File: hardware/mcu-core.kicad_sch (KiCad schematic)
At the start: 22 parts, among them SW1 B3U-1000P, U1 STM32F103C8T6, Y1 12MHz

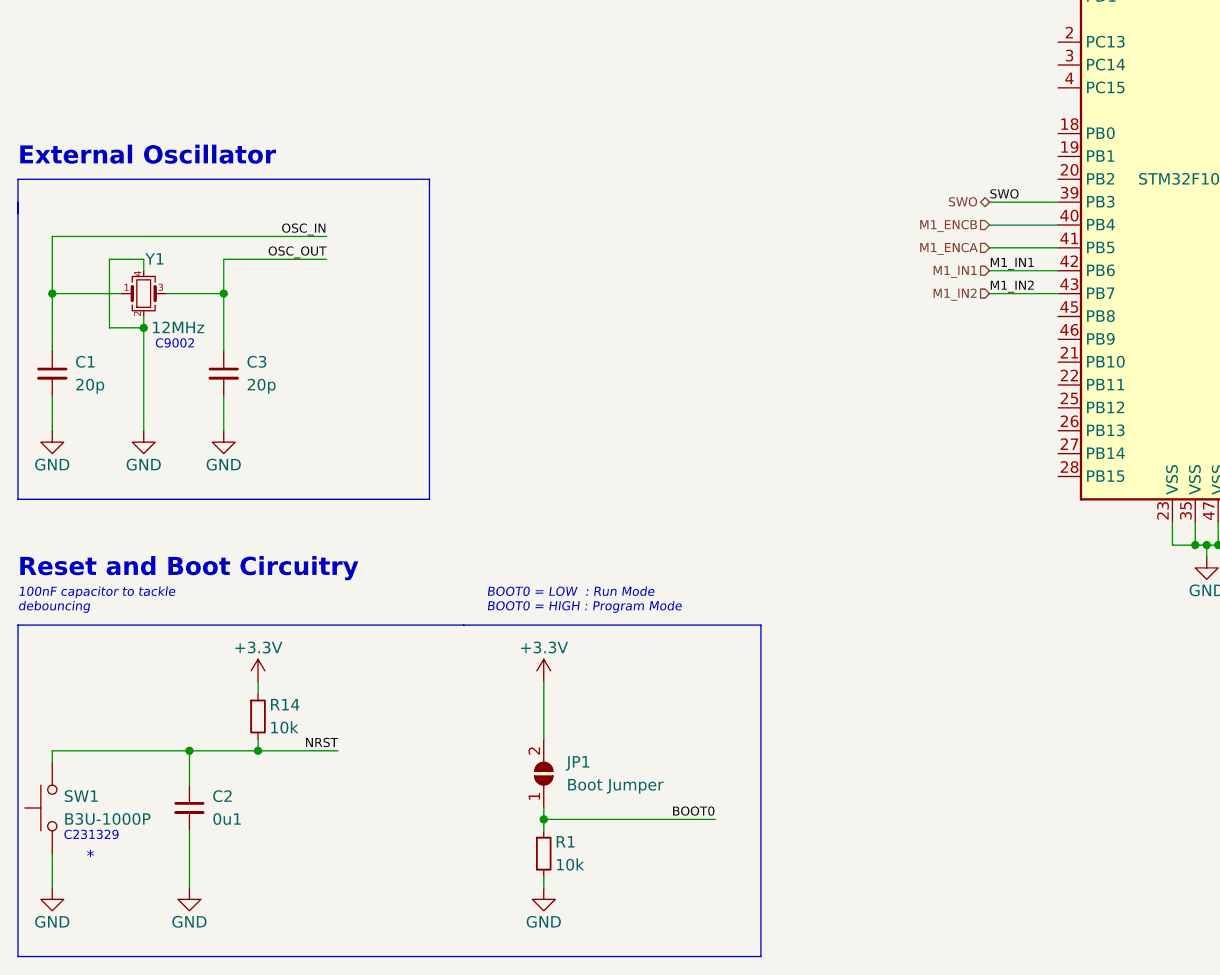
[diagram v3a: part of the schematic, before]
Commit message: Added BOOT1 jumper
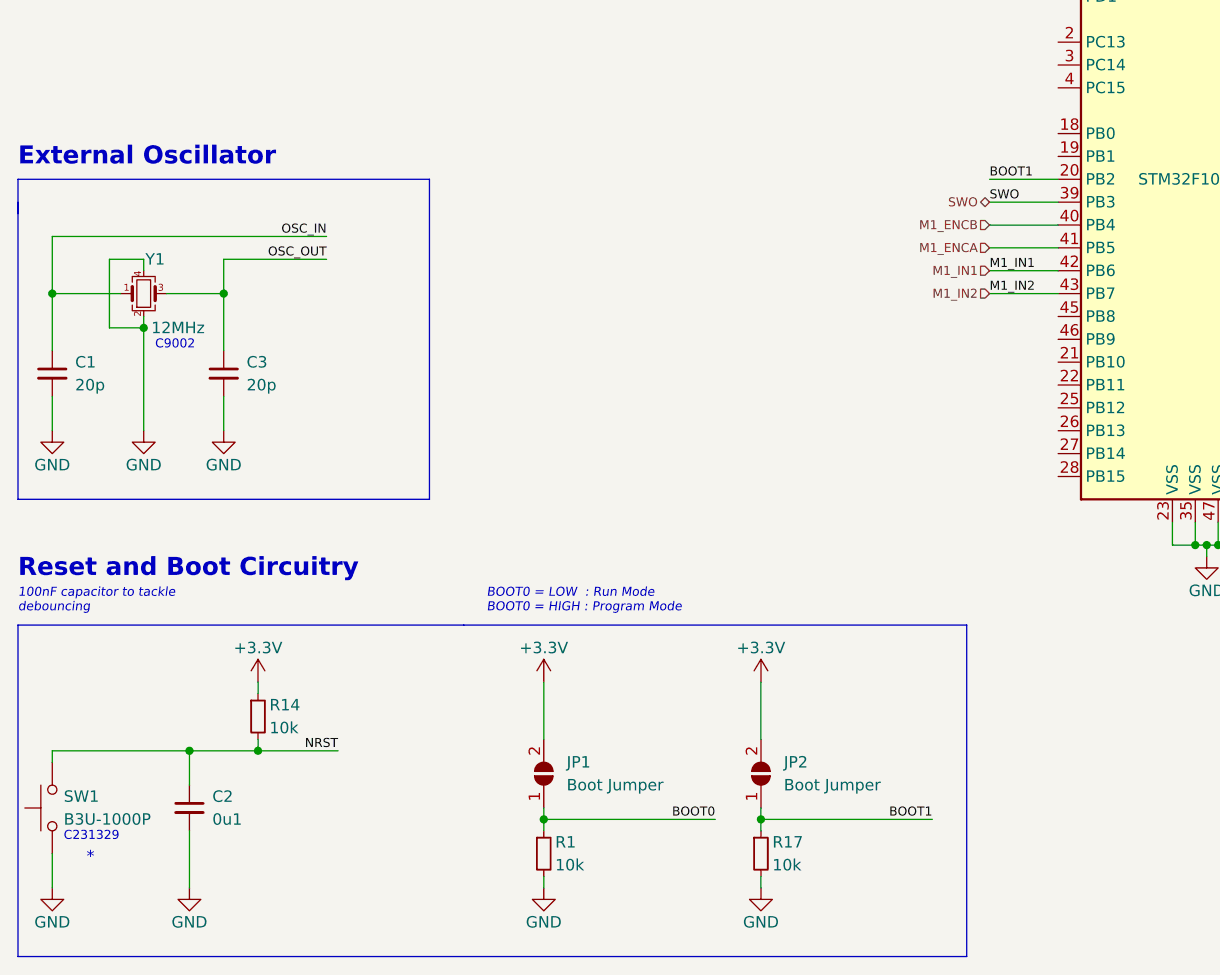
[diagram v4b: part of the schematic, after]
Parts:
- added JP2: Boot Jumper, Jumper:SolderJumper-2_P1.3mm_Open_Pad1.0x1.5mm, symbol Jumper:SolderJumper_2_Open
- added R17: 10k, Resistor_SMD:R_0402_1005Metric, symbol Device:R_Small
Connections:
- net +3.3V: now also JP2.2 (B)
- net GND: now also R17.2
- net BOOT1: now reaches U1.20 (PB2)
- net BOOT1: now also JP2.1 (A), R17.1
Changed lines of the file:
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@@
   (junction (at 125.73 66.04) (diameter 0) (color 0 0 0 0)
   )
+  (junction (at 96.52 181.61) (diameter 0) (color 0 0 0 0)
+  )
   (junction (at 40.64 173.99) (diameter 0) (color 0 0 0 0)
   )
@@
     (stroke (width 0) (type default) (color 0 0 0 0))
   )
+  (wire (pts (xy 96.52 181.61) (xy 96.52 182.88))
+    (stroke (width 0) (type default) (color 0 0 0 0))
+  )
   (wire (pts (xy 36.83 119.38) (xy 48.26 119.38))
     (stroke (width 0) (type default) (color 0 0 0 0))
@@
     (stroke (width 0) (type default) (color 0 0 0 0))
   )
+  (wire (pts (xy 96.52 181.61) (xy 115.57 181.61))
+    (stroke (width 0) (type default) (color 0 0 0 0))
+  )
   (wire (pts (xy 121.92 120.65) (xy 129.54 120.65))
     (stroke (width 0) (type default) (color 0 0 0 0))
@@
     (stroke (width 0) (type default) (color 0 0 0 0))
   )
+  (wire (pts (xy 96.52 180.34) (xy 96.52 181.61))
+    (stroke (width 0) (type default) (color 0 0 0 0))
+  )
   (wire (pts (xy 121.92 115.57) (xy 129.54 115.57))
     (stroke (width 0) (type default) (color 0 0 0 0))
@@
     (stroke (width 0) (type default) (color 0 0 0 0))
   )
-  (polyline (pts (xy 96.52 160.02) (xy 96.52 196.85))
+  (polyline (pts (xy 119.38 160.02) (xy 119.38 196.85))
     (stroke (width 0) (type default) (color 0 0 0 0))
   )
@@
     (stroke (width 0) (type default) (color 0 0 0 0))
   )
+  (wire (pts (xy 96.52 187.96) (xy 96.52 189.23))
+    (stroke (width 0) (type default) (color 0 0 0 0))
+  )
   (polyline (pts (xy 59.69 146.05) (xy 59.69 110.49))
     (stroke (width 0) (type default) (color 0 0 0 0))
   )
-  (polyline (pts (xy 63.5 160.02) (xy 96.52 160.02))
+  (polyline (pts (xy 63.5 160.02) (xy 119.38 160.02))
     (stroke (width 0) (type default) (color 0 0 0 0))
   )
@@
     (stroke (width 0) (type default) (color 0 0 0 0))
   )
+  (wire (pts (xy 96.52 166.37) (xy 96.52 172.72))
+    (stroke (width 0) (type default) (color 0 0 0 0))
+  )
   (wire (pts (xy 162.56 133.35) (xy 177.8 133.35))
     (stroke (width 0) (type default) (color 0 0 0 0))
@@
     (stroke (width 0) (type default) (color 0 0 0 0))
   )
+  (wire (pts (xy 121.92 110.49) (xy 129.54 110.49))
+    (stroke (width 0) (type default) (color 0 0 0 0))
+  )
   (wire (pts (xy 146.05 152.4) (xy 146.05 151.13))
     (stroke (width 0) (type default) (color 0 0 0 0))
@@
     (stroke (width 0) (type default) (color 0 0 0 0))
   )
-  (polyline (pts (xy 96.52 196.85) (xy 13.97 196.85))
+  (polyline (pts (xy 119.38 196.85) (xy 13.97 196.85))
     (stroke (width 0) (type default) (color 0 0 0 0))
   )
@@
     (effects (font (size 1 1)) (justify right bottom))
   )
+  (label "BOOT1" (at 121.92 110.49 0)
+    (effects (font (size 1 1)) (justify left bottom))
+  )
   (label "OSC_IN" (at 48.26 116.84 180)
     (effects (font (size 1 1)) (justify right bottom))
@@
   (label "NRST" (at 119.38 77.47 0)
     (effects (font (size 1 1)) (justify left bottom))
+  )
+  (label "BOOT1" (at 115.57 181.61 180)
+    (effects (font (size 1 1)) (justify right bottom))
   )
   (label "BOOT0" (at 91.44 181.61 180)
@@
     )
     (pin "1")
+  )
+  (symbol (lib_id "Device:R_Small") (at 96.52 185.42 0) (unit 1)
+    (in_bom yes) (on_board yes)
+    (property "Reference" "R17" (id 0) (at 97.79 184.15 0)
+      (effects (font (size 1.27 1.27)) (justify left))
+    )
+    (property "Value" "10k" (id 1) (at 97.79 186.69 0)
+      (effects (font (size 1.27 1.27)) (justify left))
+    )
+    (property "Footprint" "Resistor_SMD:R_0402_1005Metric" (id 2) (at 96.52 185.42 0)
+      (effects (font (size 1.27 1.27)) hide)
+    )
+    (property "Datasheet" "~" (id 3) (at 96.52 185.42 0)
+      (effects (font (size 1.27 1.27)) hide)
+    )
+    (pin "1")
+    (pin "2")
   )
   (symbol (lib_id "Switch:SW_Push") (at 17.78 180.34 90) (unit 1)
@@
     (pin "4")
   )
+  (symbol (lib_id "power:GND") (at 96.52 189.23 0) (unit 1)
+    (in_bom yes) (on_board yes)
+    (property "Reference" "#PWR056" (id 0) (at 96.52 195.58 0)
+      (effects (font (size 1.27 1.27)) hide)
+    )
+    (property "Value" "GND" (id 1) (at 96.52 193.04 0))
+    (property "Footprint" "" (id 2) (at 96.52 189.23 0)
+      (effects (font (size 1.27 1.27)) hide)
+    )
+    (property "Datasheet" "" (id 3) (at 96.52 189.23 0)
+      (effects (font (size 1.27 1.27)) hide)
+    )
+    (pin "1")
+  )
   (symbol (lib_id "power:+3.3V") (at 190.5 125.73 0) (unit 1)
     (in_bom yes) (on_board yes)
@@
     )
     (property "Datasheet" "~" (id 3) (at 256.54 100.33 0)
+      (effects (font (size 1.27 1.27)) hide)
+    )
+    (pin "1")
+    (pin "2")
+  )
+  (symbol (lib_id "Jumper:SolderJumper_2_Open") (at 96.52 176.53 90) (unit 1)
+    (in_bom yes) (on_board yes) (fields_autoplaced)
+    (property "Reference" "JP2" (id 0) (at 99.06 175.2599 90)
+      (effects (font (size 1.27 1.27)) (justify right))
+    )
+    (property "Value" "Boot Jumper" (id 1) (at 99.06 177.7999 90)
+      (effects (font (size 1.27 1.27)) (justify right))
+    )
+    (property "Footprint" "Jumper:SolderJumper-2_P1.3mm_Open_Pad1.0x1.5mm" (id 2) (at 96.52 176.53 0)
+      (effects (font (size 1.27 1.27)) hide)
+    )
+    (property "Datasheet" "~" (id 3) (at 96.52 176.53 0)
       (effects (font (size 1.27 1.27)) hide)
     )
@@
       (effects (font (size 1.27 1.27)) hide)
     )
+    (pin "1")
+  )
+  (symbol (lib_id "power:+3.3V") (at 96.52 166.37 0) (unit 1)
+    (in_bom yes) (on_board yes)
+    (property "Reference" "#PWR055" (id 0) (at 96.52 170.18 0)
+      (effects (font (size 1.27 1.27)) hide)
+    )
+    (property "Value" "+3.3V" (id 1) (at 96.52 162.56 0))
+    (property "Footprint" "" (id 2) (at 96.52 166.37 0)
+      (effects (font (size 1.27 1.27)) hide)
+    )
+    (property "Datasheet" "" (id 3) (at 96.52 166.37 0)
+      (effects (font (size 1.27 1.27)) hide)
+    )

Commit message: Added status LED and silkscreen
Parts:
- added D15: orange, LED_SMD:LED_0603_1608Metric, symbol Device:LED_Small_Filled
- added R18: 1k5, Resistor_SMD:R_0402_1005Metric, symbol Device:R_Small
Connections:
- net GND: now also R18.2
- net at U1.27 (PB14): now also D15.2 (A)
- new net: D15.1 (K), R18.1
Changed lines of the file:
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@@
+    (stroke (width 0) (type default) (color 0 0 0 0))
+  )
+  (wire (pts (xy 118.11 140.97) (xy 118.11 142.24))
     (stroke (width 0) (type default) (color 0 0 0 0))
   )
@@
     (stroke (width 0) (type default) (color 0 0 0 0))
   )
+  (wire (pts (xy 118.11 140.97) (xy 129.54 140.97))
+    (stroke (width 0) (type default) (color 0 0 0 0))
+  )
   (wire (pts (xy 96.52 181.61) (xy 115.57 181.61))
     (stroke (width 0) (type default) (color 0 0 0 0))
@@
     (stroke (width 0) (type default) (color 0 0 0 0))
   )
+  (wire (pts (xy 118.11 147.32) (xy 118.11 148.59))
+    (stroke (width 0) (type default) (color 0 0 0 0))
+  )
   (wire (pts (xy 144.78 151.13) (xy 142.24 151.13))
     (stroke (width 0) (type default) (color 0 0 0 0))
@@
   )
   (wire (pts (xy 101.6 66.04) (xy 101.6 67.31))
+    (stroke (width 0) (type default) (color 0 0 0 0))
+  )
+  (wire (pts (xy 118.11 153.67) (xy 118.11 154.94))
     (stroke (width 0) (type default) (color 0 0 0 0))
   )
@@
     (pin "2")
   )
+  (symbol (lib_id "Device:LED_Small_Filled") (at 118.11 144.78 90) (unit 1)
+    (in_bom yes) (on_board yes)
+    (property "Reference" "D15" (id 0) (at 113.03 143.51 90)
+      (effects (font (size 1.27 1.27)) (justify right))
+    )
+    (property "Value" "orange" (id 1) (at 110.49 147.32 90)
+      (effects (font (size 1.27 1.27)) (justify right))
+    )
+    (property "Footprint" "LED_SMD:LED_0603_1608Metric" (id 2) (at 118.11 144.78 90)
+      (effects (font (size 1.27 1.27)) hide)
+    )
+    (property "Datasheet" "~" (id 3) (at 118.11 144.78 90)
+      (effects (font (size 1.27 1.27)) hide)
+    )
+    (pin "1")
+    (pin "2")
+  )
   (symbol (lib_id "Device:R_Small") (at 72.39 185.42 0) (unit 1)
     (in_bom yes) (on_board yes)
@@
     (pin "2")
   )
+  (symbol (lib_id "power:GND") (at 118.11 154.94 0) (unit 1)
+    (in_bom yes) (on_board yes)
+    (property "Reference" "#PWR057" (id 0) (at 118.11 161.29 0)
+      (effects (font (size 1.27 1.27)) hide)
+    )
+    (property "Value" "GND" (id 1) (at 118.11 158.75 0))
+    (property "Footprint" "" (id 2) (at 118.11 154.94 0)
+      (effects (font (size 1.27 1.27)) hide)
+    )
+    (property "Datasheet" "" (id 3) (at 118.11 154.94 0)
+      (effects (font (size 1.27 1.27)) hide)
+    )
+    (pin "1")
+  )
   (symbol (lib_id "power:GND") (at 72.39 189.23 0) (unit 1)
     (in_bom yes) (on_board yes)
@@
     (pin "1")
   )
+  (symbol (lib_id "Device:R_Small") (at 118.11 151.13 0) (mirror y) (unit 1)
+    (in_bom yes) (on_board yes)
+    (property "Reference" "R18" (id 0) (at 116.84 149.86 0)
+      (effects (font (size 1.27 1.27)) (justify left))
+    )
+    (property "Value" "1k5" (id 1) (at 116.84 152.4 0)
+      (effects (font (size 1.27 1.27)) (justify left))
+    )
+    (property "Footprint" "Resistor_SMD:R_0402_1005Metric" (id 2) (at 118.11 151.13 0)
+      (effects (font (size 1.27 1.27)) hide)
+    )
+    (property "Datasheet" "~" (id 3) (at 118.11 151.13 0)
+      (effects (font (size 1.27 1.27)) hide)
+    )
+    (pin "1")
+    (pin "2")
+  )
   (symbol (lib_id "power:GND") (at 17.78 189.23 0) (unit 1)

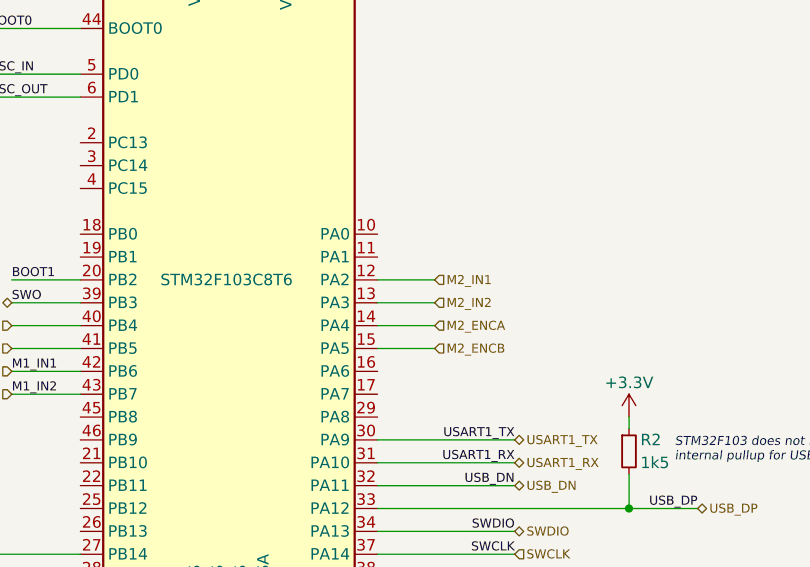
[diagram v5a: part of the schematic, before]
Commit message: Minor changes, added 100n cap
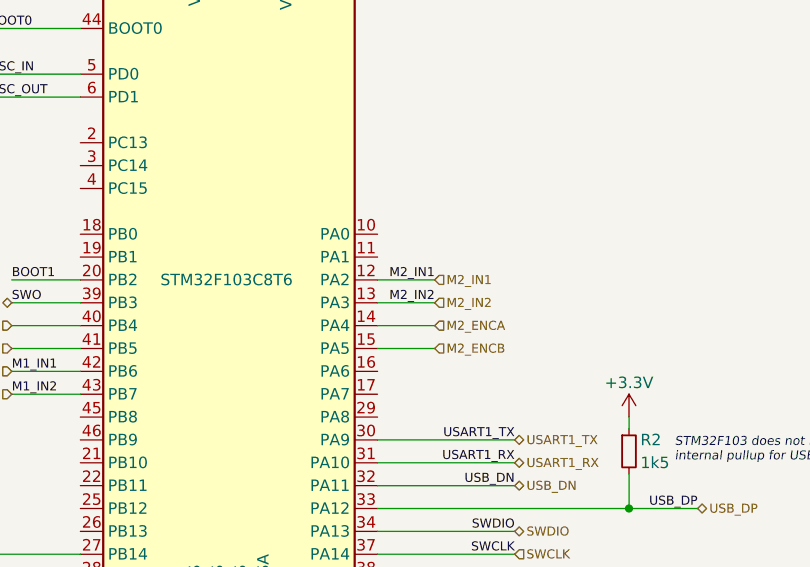
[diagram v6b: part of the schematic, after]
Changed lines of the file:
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@@
+    (effects (font (size 1 1)) (justify right bottom))
+  )
+  (label "M2_IN2" (at 168.91 113.03 180)
     (effects (font (size 1 1)) (justify right bottom))
   )
@@
     (effects (font (size 1 1)) (justify right bottom))
   )
+  (label "M2_IN1" (at 168.91 110.49 180)
+    (effects (font (size 1 1)) (justify right bottom))
+  )

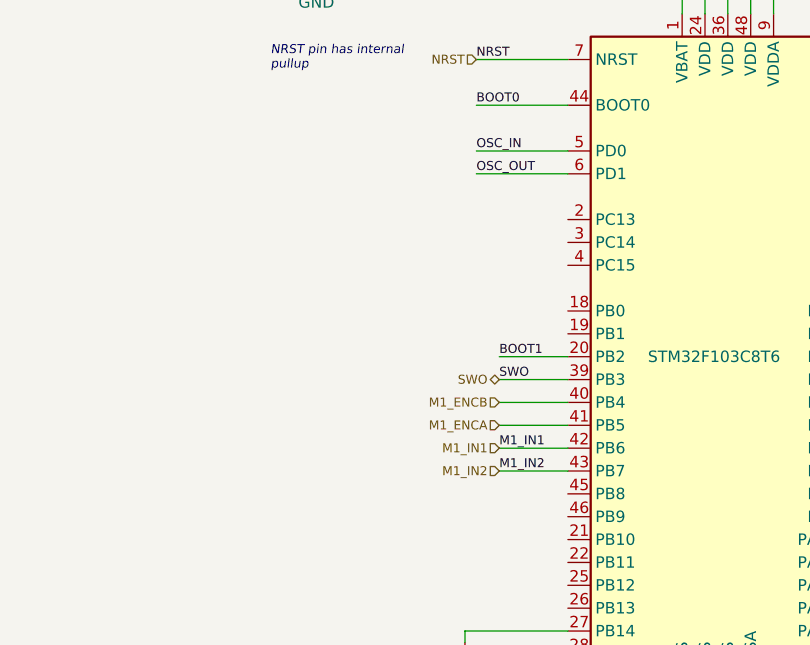
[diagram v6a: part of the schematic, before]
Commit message: Updated hardware design, added TagConnect Probe and Battery Voltage Measurement
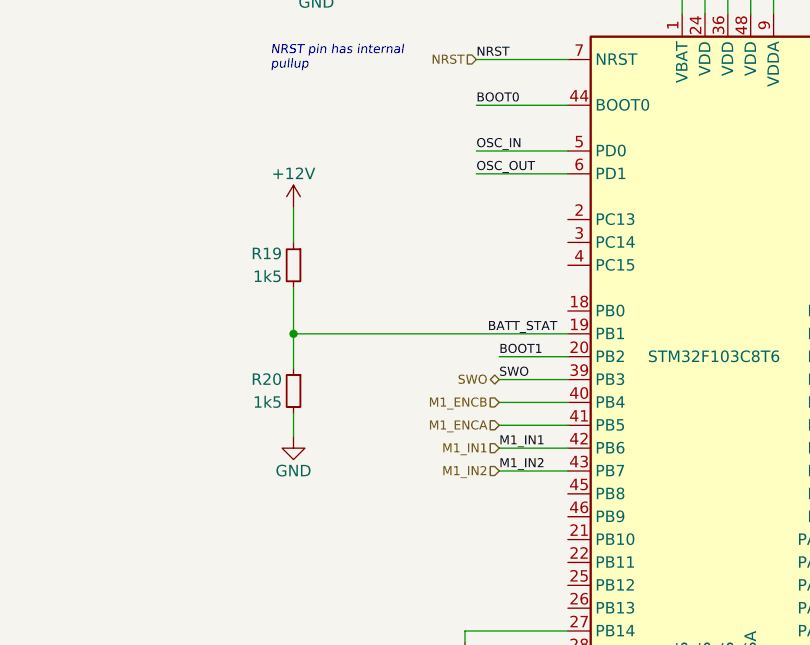
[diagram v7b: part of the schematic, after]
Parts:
- added R19, R20: 1k5, Resistor_SMD:R_0603_1608Metric_Pad0.98x0.95mm_HandSolder, symbol Device:R_Small
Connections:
- net GND: now also R20.2
- net BATT_STAT: now reaches U1.19 (PB1)
- net BATT_STAT: now also R19.2, R20.1
- new net +12V: R19.1

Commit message: Updated design, ready to generate production files
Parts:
- C10: value 0u1 -> 1u
- R19: value 1k5 -> 47k
- R20: value 1k5 -> 10k
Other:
- moved on the sheet: C4, C5, C6, C7, C8
